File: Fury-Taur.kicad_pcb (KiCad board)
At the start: 2 copper layers, 54.5 x 24 mm, 17 parts, among them Q1 J201, Q2 J201, SW1 ALPHA_PUSH_PULL

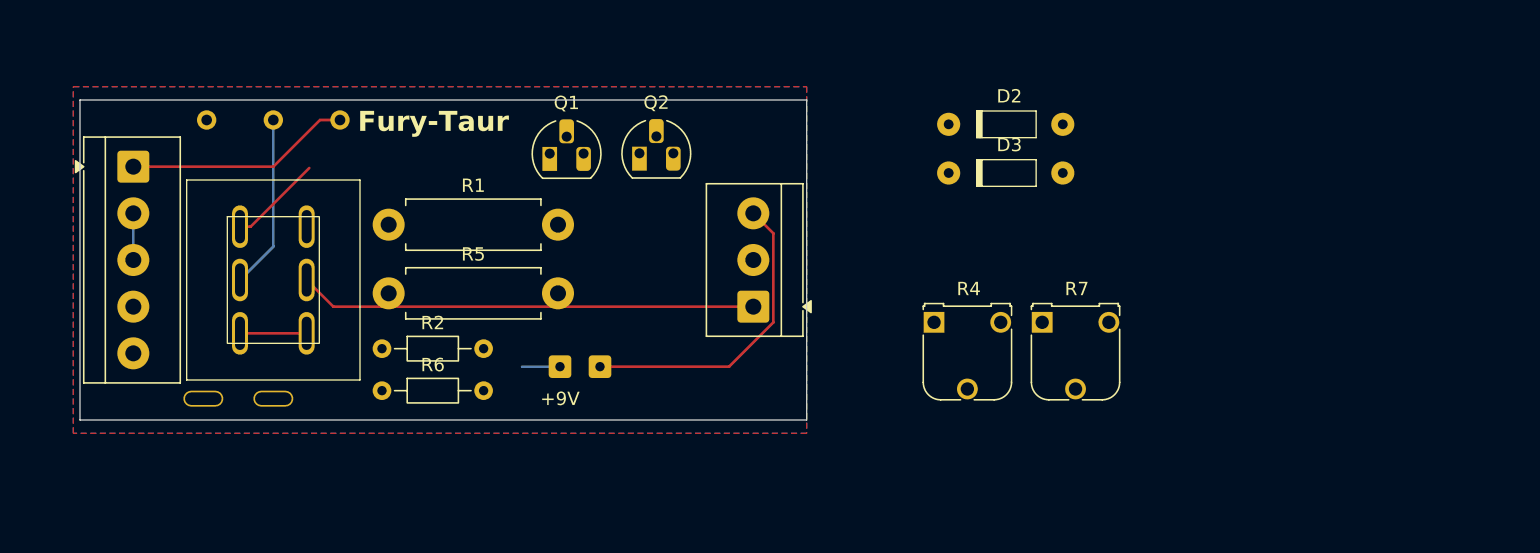
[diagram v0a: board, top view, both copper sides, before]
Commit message: Added components to PCB board
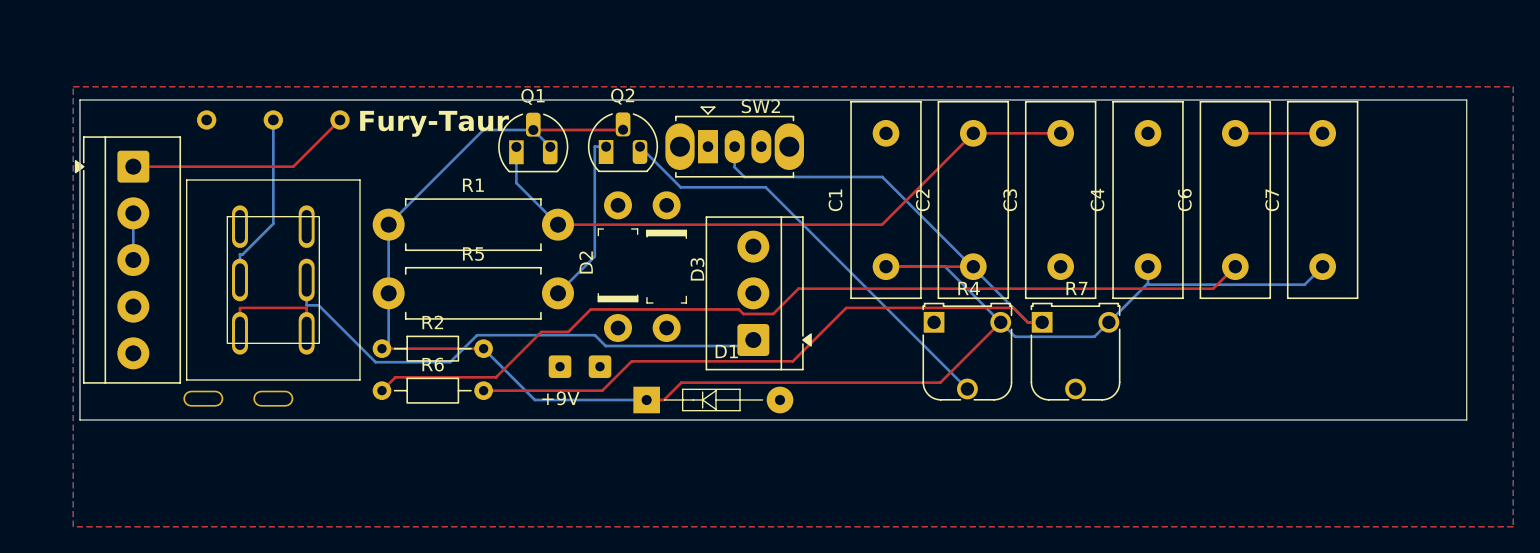
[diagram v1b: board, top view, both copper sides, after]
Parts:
- added C1: 10nf, Capacitor_THT:C_Disc_D14.5mm_W5.0mm_P10.00mm, F.Cu at (138.9, 76.5)
- added C2: 47pf, Capacitor_THT:C_Disc_D14.5mm_W5.0mm_P10.00mm, F.Cu at (145.5, 76.5)
- added C3: 4.7nf, Capacitor_THT:C_Disc_D14.5mm_W5.0mm_P10.00mm, F.Cu at (152.1, 76.5)
- added C4: 100nf, Capacitor_THT:C_Disc_D14.5mm_W5.0mm_P10.00mm, F.Cu at (158.6, 76.5)
- added C6: 10nf, Capacitor_THT:C_Disc_D14.5mm_W5.0mm_P10.00mm, F.Cu at (165.2, 76.5)
- added C7: 47pf, Capacitor_THT:C_Disc_D14.5mm_W5.0mm_P10.00mm, F.Cu at (171.7, 76.5)
- added D1: 1N5817, digikey-footprints:Diode_DO-35_P10mm, F.Cu at (121.0, 86.5)
- added SW2: SW_SPDT, Button_Switch_THT:SW_Slide_SPDT_Straight_CK_OS102011MS2Q, F.Cu at (125.6, 67.5)
- D2, D3: footprint digikey-footprints:DO-35 -> digikey-footprints:DO-41
- moved D2 29.1 mm to (118.8, 81.0), turned to 90 degrees
- moved D3 21.3 mm to (122.5, 71.9), turned to -90 degrees
- moved Q1 2.55 mm to (111.2, 67.5)
- moved Q2 2.55 mm to (118.0, 67.5)
- moved Output 2.50 mm to (129.0, 82.0)
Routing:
- net Net-(D1-K): track 0.00 -> 127.3 mm
- net Net-(SW2-B): track 0.00 -> 74.3 mm
- net Net-(C6-Pad1): track 0.00 -> 68.1 mm
- net Net-(Q1-D): track 0.00 -> 47.7 mm
- net Net-(Q2-G): track 0.00 -> 32.1 mm
- net GND: track 23.2 -> 0.00 mm
- net Net-(Q2-D): track 0.00 -> 19.5 mm
- net GATE: track 7.02 -> 0.00 mm
- net VOL_OUT_TO_JACK_TIP: track 34.3 -> 38.5 mm
- net COMMON: track 5.00 -> 8.80 mm
- net 9V_IN: track 2.84 -> 0.00 mm
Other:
- board size 54.5 x 24 mm -> 104 x 24 mm

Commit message: Rearranged PCB, added footprints
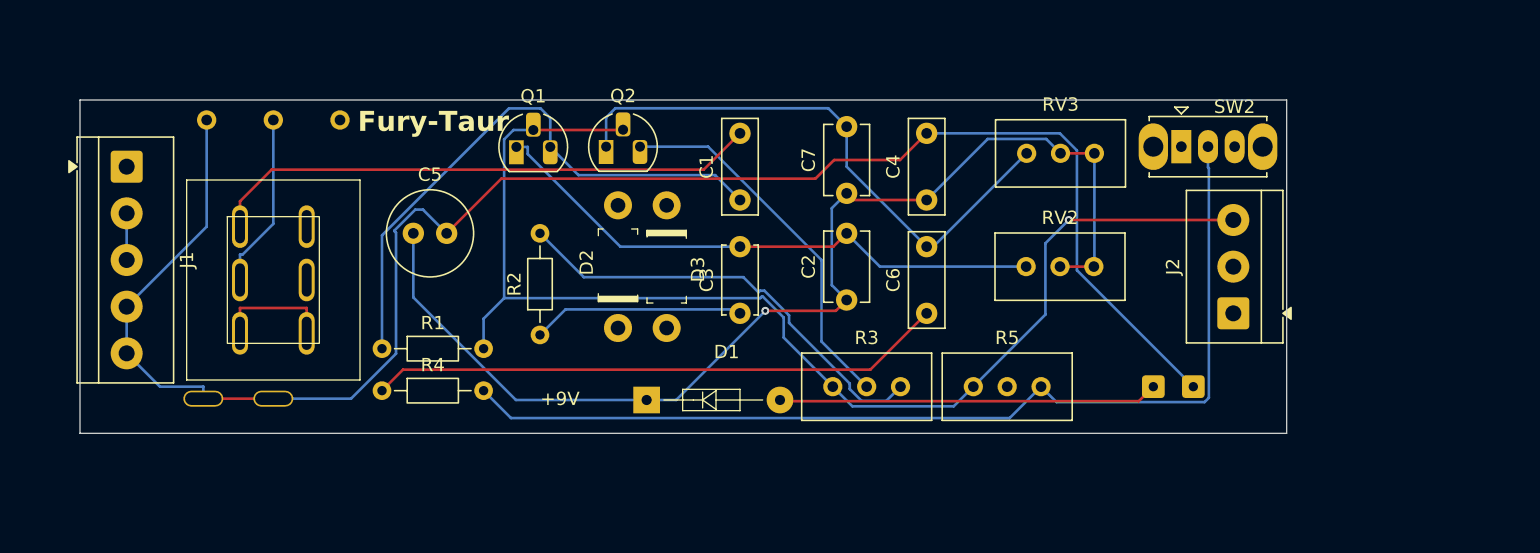
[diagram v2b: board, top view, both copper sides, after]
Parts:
- removed Input: TerminalBlock_4Ucon_1x05_P3.50mm_Horizontal, TerminalBlock_4Ucon:TerminalBlock_4Ucon_1x05_P3.50mm_Horizontal
- removed Output: TerminalBlock_4Ucon_1x03_P3.50mm_Horizontal, TerminalBlock_4Ucon:TerminalBlock_4Ucon_1x03_P3.50mm_Horizontal
- removed the R1 at (101.7, 73.3)
- removed the R5 at (101.7, 78.5)
- added C5: 220uf, Capacitor_THT:C_Radial_D6.3mm_H11.0mm_P2.50mm, F.Cu at (103.5, 74.0)
- added J1: Pickup, TerminalBlock_4Ucon:TerminalBlock_4Ucon_1x05_P3.50mm_Horizontal, F.Cu at (82.0, 69.0)
- added J2: Output, TerminalBlock_4Ucon:TerminalBlock_4Ucon_1x03_P3.50mm_Horizontal, F.Cu at (165.0, 80.0)
- added R2: 33K, Resistor_THT:R_Axial_DIN0204_L3.6mm_D1.6mm_P7.62mm_Horizontal, F.Cu at (113.0, 81.6)
- added RV2: 20K, Potentiometer_THT:Potentiometer_Bourns_3296W_Vertical, F.Cu at (154.5, 76.5)
- added RV3: 20K, Potentiometer_THT:Potentiometer_Bourns_3296W_Vertical, F.Cu at (154.6, 68.0)
- C1, C4, C6: footprint Capacitor_THT:C_Disc_D14.5mm_W5.0mm_P10.00mm -> Capacitor_THT:C_Disc_D7.0mm_W2.5mm_P5.00mm
- C2, C7: footprint Capacitor_THT:C_Disc_D14.5mm_W5.0mm_P10.00mm -> Capacitor_THT:C_Disc_D5.1mm_W3.2mm_P5.00mm
- C3: footprint Capacitor_THT:C_Disc_D14.5mm_W5.0mm_P10.00mm -> Capacitor_THT:C_Disc_D5.0mm_W2.5mm_P5.00mm
- R3: renamed from R4; footprint Potentiometer_THT:Potentiometer_Runtron_RM-065_Vertical -> Potentiometer_THT:Potentiometer_Bourns_3296W_Vertical
- R5: renamed from R7; footprint Potentiometer_THT:Potentiometer_Runtron_RM-065_Vertical -> Potentiometer_THT:Potentiometer_Bourns_3296W_Vertical
- moved 9V+ 44.5 mm to (159.0, 85.5)
- moved 9V- 44.5 mm to (162.0, 85.5)
- moved C7 36.1 mm to (136.0, 71.0)
- moved SW2 35.5 mm to (161.1, 67.5)
- moved C3 24.3 mm to (128.0, 80.0)
- moved C6 23.4 mm to (142.0, 80.0)
- moved C4 17.3 mm to (142.0, 71.5)
- moved C1 12.0 mm to (128.0, 71.5)
- moved C2 9.82 mm to (136.0, 79.0)
- moved R3 5.44 mm to (140.0, 85.5)
- moved R5 4.83 mm to (150.6, 85.5)
- renumbered R2 to R1, R6 to R4
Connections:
- 9V+ pad 1: 9V_IN -> +9V
- C1 pad 1: Net-(D1-K) -> Net-(Q1-G)
- Q1 pad 2: Net-(D1-K) -> Net-(D2-K)
- Q1 pad 3: Net-(D1-K) -> Net-(Q1-G)
- Q2 pad 2: Net-(D1-K) -> Net-(D2-K)
- R1 pad 1: Net-(D1-K) -> Net-(Q1-G)
- R1 pad 2: Net-(D1-K) -> Net-(D2-K)
- R3 pad 3: Net-(D1-K) -> Net-(D2-K)
- R5 pad 3: Net-(D1-K) -> Net-(D2-K)
- SW1 pad 4: GATE -> Net-(C1-Pad2)
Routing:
- net GND: track 0.00 -> 130.3 mm
- net Net-(D2-K): track 0.00 -> 93.5 mm, vias 0 -> 1
- net Net-(Q1-G): track 0.00 -> 43.4 mm
- net Net-(D1-K): track 127.3 -> 84.7 mm, vias 0 -> 1
- net Net-(C1-Pad2): track 0.00 -> 41.5 mm
- net VOL_OUT_TO_JACK_TIP: track 38.5 -> 0.00 mm
- net Net-(R2-Pad2): track 0.00 -> 33.4 mm
- net +9V: track 0.00 -> 28.5 mm
- net Net-(C6-Pad1): track 68.1 -> 43.3 mm
- net Net-(Q2-D): track 19.5 -> 43.0 mm
- net PU_NORTH_START: track 16.9 -> 0.00 mm
- net Net-(C3-Pad1): track 0.00 -> 15.9 mm
- net Net-(Q1-D): track 47.7 -> 43.1 mm
- net Net-(Q2-G): track 32.1 -> 28.0 mm
- net WhiteRed: track 3.50 -> 0.00 mm
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- removed copper zone on B.Cu, net GND
- removed copper zone on F.Cu, net GND
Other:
- board size 104 x 24 mm -> 90.5 x 25 mm

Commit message: Rearranged PCB, added footprints, sanity checked net q
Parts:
- moved RV2 34.8 mm to (121.1, 86.0)
- moved D1 29.0 mm to (145.5, 71.0), turned to -90 degrees
- moved RV3 28.5 mm to (132.5, 86.0)
- moved R4 26.5 mm to (124.0, 72.4), turned to -90 degrees
- moved SW2 26.2 mm to (142.5, 86.0), turned to 180 degrees
- moved C6 21.8 mm to (121.5, 72.5), turned to 180 degrees
- moved C1 20.6 mm to (107.5, 70.5), turned to 180 degrees
- moved R3 19.2 mm to (143.0, 66.5)
- moved R5 19.2 mm to (153.6, 66.5)
- moved D2 18.0 mm to (136.8, 81.1)
- moved D3 18.0 mm to (140.5, 72.0)
- moved C3 17.9 mm to (111.5, 73.0)
- moved C4 16.1 mm to (126.5, 67.0), turned to 180 degrees
- moved C2 15.0 mm to (121.0, 78.0), turned to 180 degrees
- moved Q2 12.8 mm to (130.7, 67.3)
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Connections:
- net Net-(J1-Pin_3) renamed Red-White
- 9V- pad 1: GND -> BAT-
- D2 pad A: (no net) -> Net-(D2-A)
- D2 pad K: (no net) -> GND
- D3 pad A: (no net) -> GND
- D3 pad K: (no net) -> Net-(D2-A)
- J1 pad 5: Net-(J1-Pin_5) -> PU_NORTH_START
- J2 pad 1: Net-(J2-Pin_1) -> VOL_OUT_TO_JACK_TIP
- J2 pad 2: BAT - -> BAT-
- SW1 pad 7: R2TOR3 -> Net-(R5-Pad2)
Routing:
- net GND: track 130.3 -> 0.00 mm, vias 0 -> 2
- net VOL_OUT_TO_JACK_TIP: track 0.00 -> 60.6 mm
- net Net-(R5-Pad2): track 0.00 -> 59.6 mm
- net Net-(C6-Pad1): track 43.3 -> 2.38 mm
- net Net-(D2-K): track 93.5 -> 56.6 mm, vias 1 -> 0
- net Net-(C1-Pad2): track 41.5 -> 14.3 mm
- net Net-(SW2-B): track 75.7 -> 48.6 mm
- net Net-(Q1-G): track 43.4 -> 20.2 mm
- net +9V: track 28.5 -> 7.36 mm
- net Net-(Q2-G): track 28.0 -> 7.36 mm
- net Net-(Q1-D): track 43.1 -> 23.3 mm
- net Net-(D2-A): track 0.00 -> 18.5 mm
- net PU_NORTH_START: track 0.00 -> 17.4 mm
- net Net-(D1-K): track 84.7 -> 73.7 mm, vias 1 -> 0
- net BAT-: track 0.00 -> 10.1 mm
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- added copper zone on B.Cu, net GND
- added copper zone on F.Cu, net GND
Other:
- board size 90.5 x 25 mm -> 78 x 25 mm

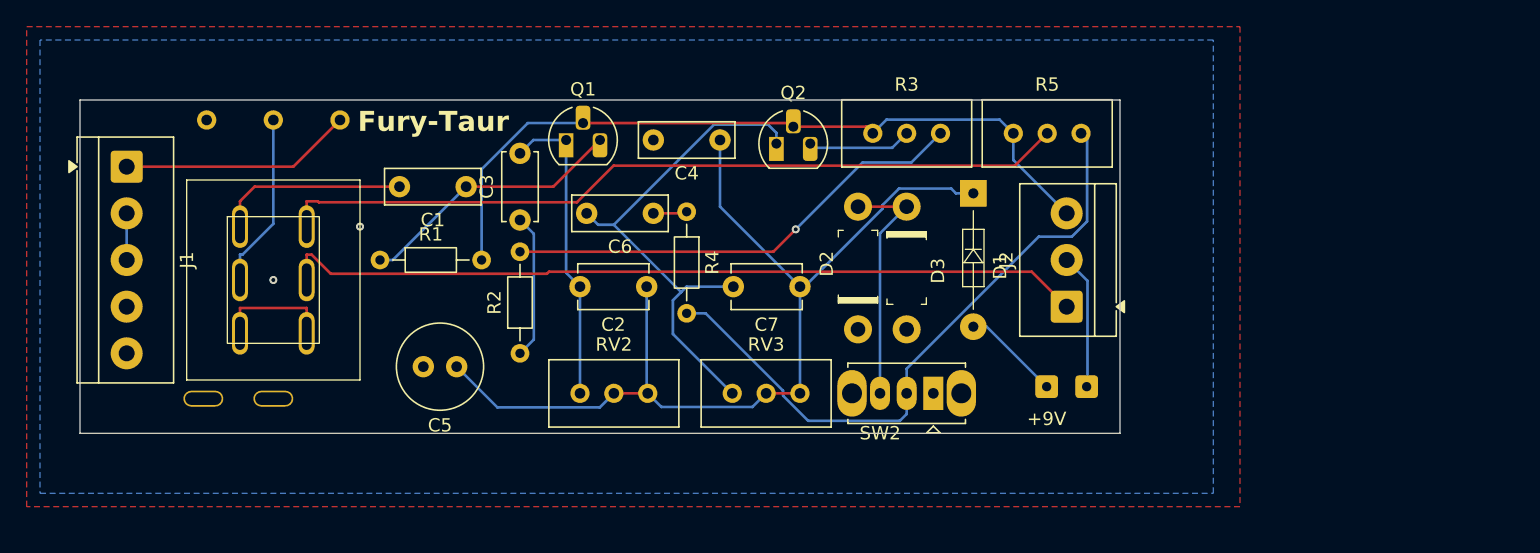
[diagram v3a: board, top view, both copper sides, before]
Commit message: Updated Silkscreens
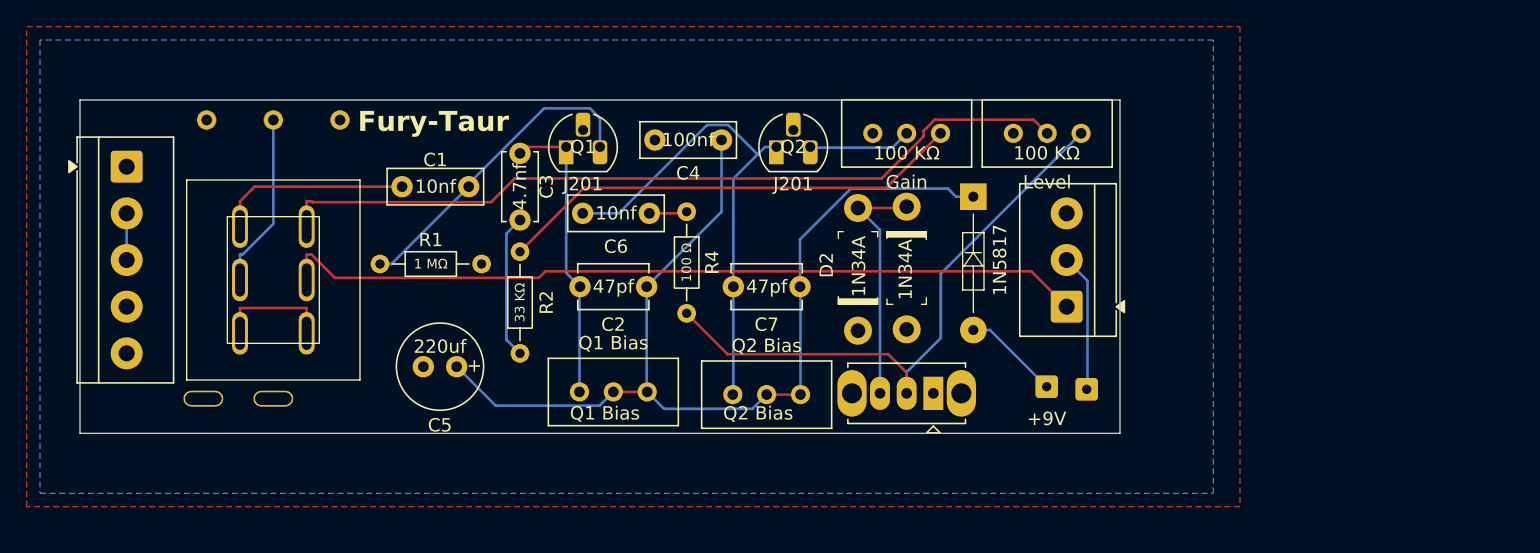
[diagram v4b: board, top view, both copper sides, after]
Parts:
- Q1 Bias: renamed from RV2
- Q2 Bias: renamed from RV3
- R3: value 100K A -> Gain
- R5: value 100K A -> Level
- moved Q1 0.52 mm to (115.0, 67.5)
- moved C6 0.30 mm to (121.2, 72.5)
- moved R1 0.30 mm to (101.0, 76.3)
- moved D1 0.25 mm to (145.5, 71.2)
- moved Q2 0.25 mm to (130.7, 67.5)
- moved C1 0.20 mm to (107.7, 70.5)
- moved C4 0.11 mm to (126.6, 67.0)
- moved Q1 Bias 0.11 mm to (121.0, 85.9)
- moved Q2 Bias 0.10 mm to (132.5, 86.1)
- moved D2 0.10 mm to (136.8, 81.2)
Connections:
- net BAT- renamed BAT -
- net Red-White renamed Net-(J1-Pin_3)
- J1 pad 5: PU_NORTH_START -> Net-(J1-Pin_5)
- J2 pad 3: Net-(D2-K) -> GND
- Q1 pad 2: Net-(D2-K) -> GND
- Q2 pad 2: Net-(D2-K) -> GND
- R1 pad 2: Net-(D2-K) -> GND
- R3 pad 3: Net-(D2-K) -> GND
- R5 pad 3: Net-(D2-K) -> GND
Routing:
- net Net-(D2-K): track 56.6 -> 0.00 mm
- net PU_NORTH_START: track 17.4 -> 0.00 mm
- net Net-(SW2-B): track 48.6 -> 44.8 mm
- net Net-(Q1-G): track 20.2 -> 23.9 mm
- net Net-(Q2-D): track 39.7 -> 37.2 mm
- net Net-(D1-K): track 73.7 -> 76.1 mm
- net Net-(R5-Pad2): track 59.6 -> 60.7 mm
- net Net-(Q1-D): track 23.3 -> 22.5 mm
- net Net-(R2-Pad2): vias 1 -> 0
- net GND: vias 2 -> 0
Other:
- board text added: "+"

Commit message: Added Strain Relief to 9V
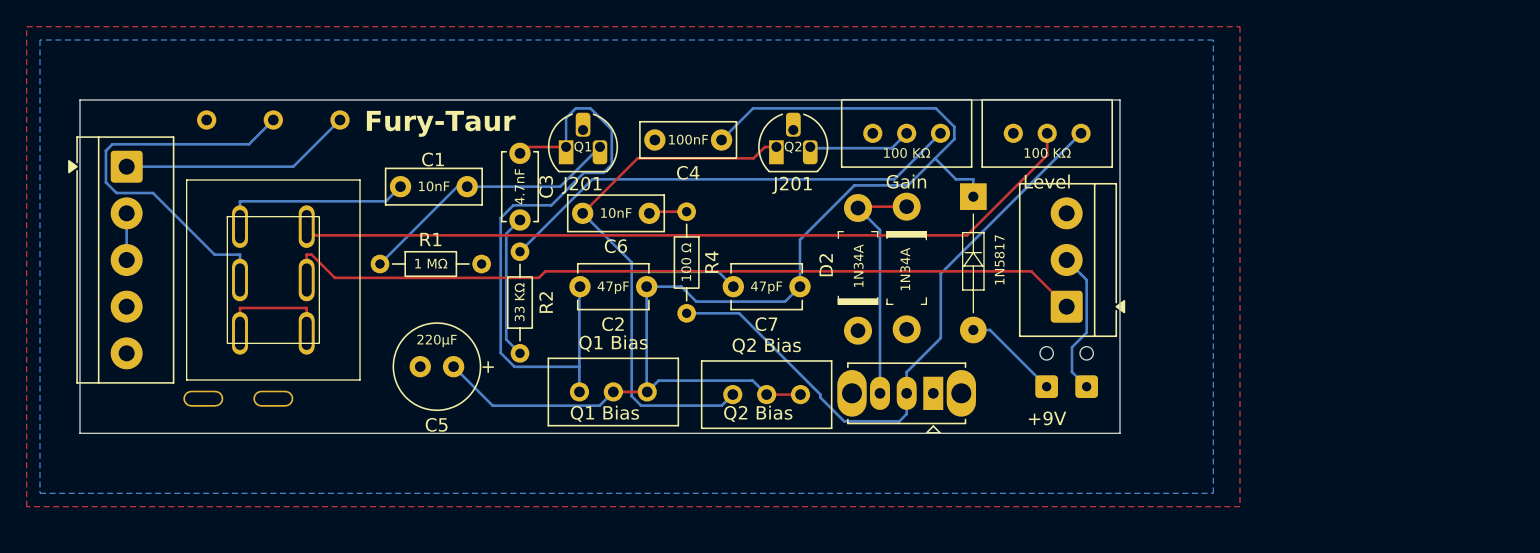
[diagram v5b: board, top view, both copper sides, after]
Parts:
- C5: value 220uf -> 220μF
- moved C5 0.23 mm to (106.5, 84.0)
- moved 9V- 0.20 mm to (154.0, 85.3)
- moved C1 0.11 mm to (107.5, 70.5)
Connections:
- J1 pad 5: Net-(J1-Pin_5) -> PU_NORTH_START
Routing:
- net Net-(Q1-D): track 22.5 -> 47.9 mm
- net PU_NORTH_START: track 0.00 -> 17.4 mm
- net VOL_OUT_TO_SWITCH: track 13.1 -> 30.1 mm
- net Net-(D1-K): track 76.1 -> 91.7 mm
- net Net-(Q2-D): track 37.2 -> 48.1 mm
- net Net-(Q1-G): track 23.9 -> 20.1 mm
- net Net-(SW2-B): track 44.8 -> 46.7 mm
- net Net-(R5-Pad2): track 60.7 -> 59.9 mm
- net BAT -: track 10.4 -> 11.0 mm
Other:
- outline, holes or cut-outs redrawn

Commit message: Changed footprints for Diodes
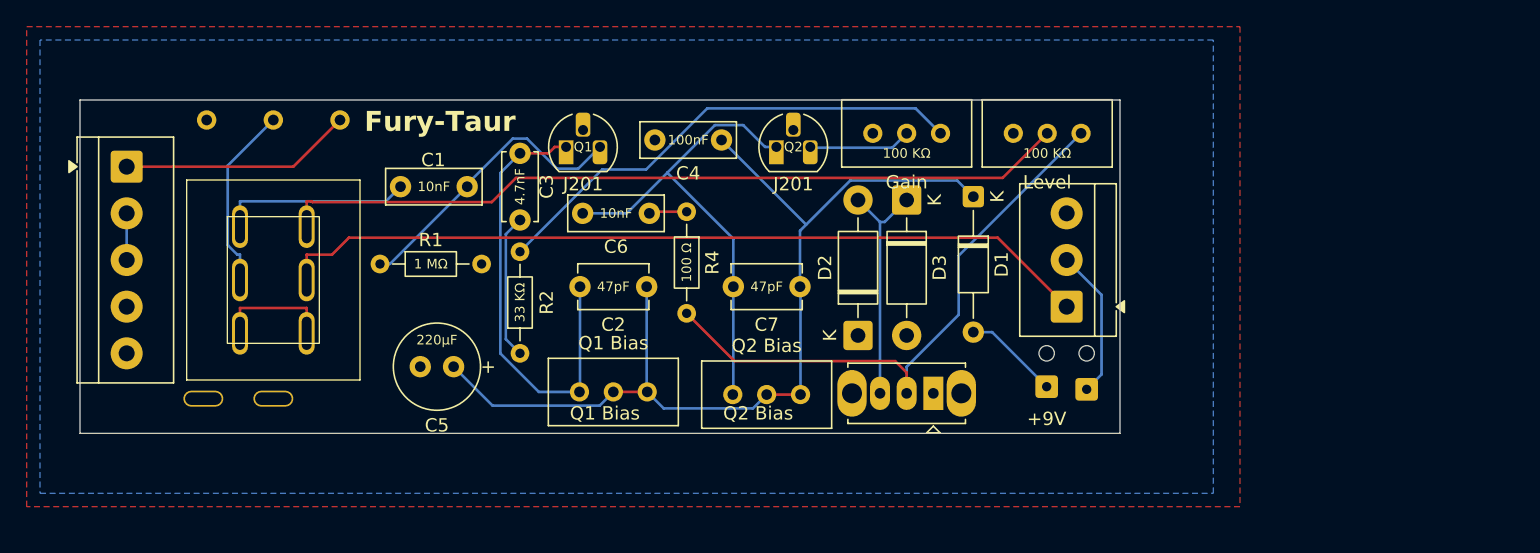
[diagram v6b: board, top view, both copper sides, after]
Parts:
- added TH1: ToolingHole_1.152mm, MountingHole:ToolingHole_1.152mm, F.Cu at (151.0, 83.0)
- added TH2: ToolingHole_1.152mm, MountingHole:ToolingHole_1.152mm, F.Cu at (154.0, 83.0)
- D1: footprint digikey-footprints:Diode_DO-35_P10mm -> Diode_THT:D_DO-35_SOD27_P10.16mm_Horizontal
- D2, D3: footprint digikey-footprints:DO-41 -> Diode_THT:D_DO-41_SOD81_P10.16mm_Horizontal
- moved D3 0.50 mm to (140.5, 71.5)
- moved D2 0.46 mm to (136.8, 81.7)
- moved 9V- 0.20 mm to (154.0, 85.5)
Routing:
- net Net-(D1-K): track 91.7 -> 72.8 mm
- net VOL_OUT_TO_SWITCH: track 30.1 -> 13.9 mm
- net Net-(Q1-D): track 47.9 -> 34.3 mm
- net Net-(Q2-D): track 48.1 -> 36.7 mm
- net Net-(Q1-G): track 20.1 -> 22.1 mm
- net Net-(SW2-B): track 46.7 -> 44.8 mm
- net Net-(R2-Pad2): track 35.2 -> 36.8 mm
- net VOL_OUT_TO_JACK_TIP: track 60.9 -> 61.6 mm
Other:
- outline, holes or cut-outs redrawn
